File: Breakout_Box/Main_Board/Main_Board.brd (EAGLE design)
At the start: 60 x 100 mm, 18 parts, among them CN1 19PIN_LEMO

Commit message: Licenses
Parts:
- added U$1: TH-PAD-1.6/0.8, CYCFI_Con:TH-PAD-1.6/0.8
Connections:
- net AGND: now also U$1.1
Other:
- board text added: "H14"
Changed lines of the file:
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@@
 <board>
 <plain>
-<wire x1="0" y1="0" x2="60" y2="0" width="0" layer="20"/>
-<wire x1="60" y1="0" x2="60" y2="100" width="0" layer="20"/>
-<wire x1="60" y1="100" x2="0" y2="100" width="0" layer="20"/>
-<wire x1="0" y1="100" x2="0" y2="0" width="0" layer="20"/>
+<wire x1="0" y1="0" x2="60" y2="0" width="0.1" layer="20"/>
+<wire x1="60" y1="0" x2="60" y2="100" width="0.1" layer="20"/>
+<wire x1="60" y1="100" x2="0" y2="100" width="0.1" layer="20"/>
+<wire x1="0" y1="100" x2="0" y2="0" width="0.1" layer="20"/>
 <text x="53.5" y="16.8" size="0.8128" layer="25" ratio="10">+</text>
 <text x="53.5" y="14.4" size="0.8128" layer="25" ratio="10">-</text>
@@
 <text x="9.70000625" y="5.6999875" size="0.8128" layer="125" ratio="10">LED1</text>
 <text x="7.114996875" y="11.562003125" size="0.8128" layer="125" ratio="10">R2</text>
+<text x="52.95" y="12.795" size="0.8128" layer="25" ratio="10" distance="46">H14</text>
 </plain>
 <attributes>
@@
 <attribute name="NAME" x="47.0225" y="14.975" size="0.8128" layer="21" ratio="10"/>
 </element>
+<element name="U$1" library="CYCFI_Con" package="TH-PAD-1.6/0.8" value="TH-PAD-1.6/0.8" x="13.5" y="3.5" smashed="yes">
+<attribute name="VALUE" x="13.5" y="4.1" size="0.0254" layer="27"/>
+</element>
 </elements>
 <signals>
@@
 <wire x1="10.75" y1="14.5" x2="12.25" y2="13" width="0.4064" layer="1"/>
 <wire x1="12.25" y1="13" x2="20" y2="13" width="0.4064" layer="1"/>
+<contactref element="U$1" pad="1"/>
 </signal>
 <signal name="DGND">

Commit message: *Edit Logo *Check BOM *Added 19P Connector Files
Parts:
- GND: value TH-PAD-1.6/0.8 -> (none)
- renumbered U$1 to GND
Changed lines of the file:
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@@
 <attribute name="NAME" x="47.0225" y="14.975" size="0.8128" layer="21" ratio="10"/>
 </element>
-<element name="U$1" library="CYCFI_Con" package="TH-PAD-1.6/0.8" value="TH-PAD-1.6/0.8" x="13.5" y="3.5" smashed="yes">
+<element name="GND" library="CYCFI_Con" package="TH-PAD-1.6/0.8" value="" x="13.5" y="3.5" smashed="yes">
 <attribute name="VALUE" x="13.5" y="4.1" size="0.0254" layer="27"/>
 </element>
@@
 <wire x1="10.75" y1="14.5" x2="12.25" y2="13" width="0.4064" layer="1"/>
 <wire x1="12.25" y1="13" x2="20" y2="13" width="0.4064" layer="1"/>
-<contactref element="U$1" pad="1"/>
+<contactref element="GND" pad="1"/>
 </signal>
 <signal name="DGND">

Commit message: reset devel
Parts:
- added C1, C3: 22uF, resistor:C0805
- added C4: 1uF, resistor:C0603
- added C5: 10uF, resistor:C0603
- added C7: 1nF, resistor:C0402K
- added H3, H4, H5: (no value), con-lstb:MA03-1_
- added L2: 82uH, resistor:L1280
- added Q1: DMP3099L, CYCFI_semicon:SOT23
- added Q2: DSS6060, CYCFI_semicon:SOT-223-4
- added R1: 1k, resistor:R0402
- C2: value 0.1uF -> 470uF; device resistor:C0603 -> resistor:140CLH-1010
- D1: value FM4007W -> FM4004W
- L1: value 100uH -> 1mH; device resistor:L1280 -> inductors:SDR
- moved D1 47.3 mm to (32.5, 60.8), turned to 90 degrees
- moved H1 45.6 mm to (50.0, 71.0)
- moved H2 45.6 mm to (9.00, 71.0)
- moved C2 42.4 mm to (28.3, 49.6), turned to 0 degrees
- moved L1 30.2 mm to (43.0, 36.5), turned to 90 degrees
- moved H13 28.7 mm to (12.8, 29.8), turned to 0 degrees
- moved C6 27.9 mm to (29.2, 24.5)
- moved H12 25.3 mm to (12.8, 27.0), turned to 0 degrees
- moved H11 22.2 mm to (12.8, 24.2), turned to 0 degrees
- moved H8 20.0 mm to (57.0, 103.2)
- moved H9 20.0 mm to (57.0, 81.8)
- moved H10 19.3 mm to (12.8, 21.5), turned to 0 degrees
- moved H6 18.0 mm to (17.5, 112.5)
- moved H7 18.0 mm to (39.0, 112.5)
- moved H14 17.0 mm to (56.0, 33.0)
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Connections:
- removed net +12V_REG: C2.1, C6.+, CN1.P$16, H1.10, H1.11, H1.8, H1.9, H9.1, H9.2, H9.3, H9.4, L1.P$2, R2.1
- removed net AGND: C2.2, C6.-, CN1.P$19, GND.1, H1.16, H1.17, H1.18, H1.19, H14.1, H7.5, H7.6, H7.7, H7.8, LED1.K
- removed net DGND: H1.12, H1.13, H1.14, H1.15, H9.5, H9.6, H9.7, H9.8
- removed net N$22: H2.19
- removed net N$23: H2.20
- removed net N$24: H1.20
- removed net N$26 (its old number): CN1.P$18
- removed net N$31: D1.CATHODE, L1.P$1
- removed net N$60: CN1.P$13, H1.5, H8.5
- removed net N$61: CN1.P$14, H1.6, H8.6
- removed net N$62: CN1.P$15, H1.7, H8.7
- removed net N$9 (its old number): CN1.P$17
- new net +AVCC: C4.1, C5.1, C7.1, CN1.P$16, CN1.P$17, D1.ANODE, H1.14, H1.15, H9.1, H9.2, Q2.P$3, R2.1
- new net +DVCC: C3.1, H1.8, H1.9, H9.5, H9.6, L1.P$2
- new net GND: C1.2, C2.-, C3.2, C4.2, C5.2, C6.-, C7.2, CN1.P$18, CN1.P$19, GND.1, H1.10, H1.11, H1.12, H1.13, H1.16, H1.17, H1.18, H1.19, H14.1, H2.16, H2.17, H2.18, H2.19, H2.20, H7.5, H7.6, H7.7, H7.8, H9.3, H9.4, H9.7, H9.8, LED1.K, Q1.1
- new net N$33: H1.5, H3.3, H8.5
- new net N$34: H1.6, H4.3, H8.6
- new net N$35: H1.7, H5.3, H8.7
- new net N$36: CN1.P$13, H3.2
- new net N$37: CN1.P$14, H4.2
- new net N$38: CN1.P$15, H5.2
- net N$1: now also H3.1
- net N$17: now also H5.1
- net N$19: now also C1.1, L1.P$1, L2.P$1, Q1.2; no longer H2.16
- net N$2: now also Q1.3; no longer D1.ANODE
- net N$20: now also C2.+, Q2.P$1, R1.1; no longer H2.17
- net N$21: now also C6.+, D1.CATHODE, L2.P$2, Q2.P$2, Q2.P$4, R1.2; no longer H2.18
- net N$3: now also H4.1
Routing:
- net N$17: track 0.00 -> 208.6 mm
- net N$3: track 0.00 -> 207.4 mm
- net N$1: track 0.00 -> 201.4 mm
- net +12V_REG: track 195.9 -> 0.00 mm, vias 1 -> 0
- net N$35: track 0.00 -> 179.9 mm, vias 0 -> 1
- net N$34: track 0.00 -> 175.0 mm, vias 0 -> 1
- net +AVCC: track 0.00 -> 169.7 mm, vias 0 -> 1
- net N$33: track 0.00 -> 169.7 mm, vias 0 -> 1
- net N$60: track 117.6 -> 0.00 mm, vias 2 -> 0
- net N$61: track 116.7 -> 0.00 mm, vias 2 -> 0
- net N$62: track 114.9 -> 0.00 mm
- net N$28: track 100.4 -> 197.6 mm, vias 1 -> 0
- net N$29: track 110.9 -> 191.9 mm, vias 1 -> 0
- net N$37: track 0.00 -> 72.6 mm, vias 0 -> 1
- net N$18: track 115.3 -> 187.2 mm, vias 1 -> 0
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- added copper zone on layer 16, net GND
- added copper zone on layer 16, net N$22
- added copper zone on layer 16, net N$23
- removed copper zone on layer 1, net AGND
- removed copper zone on layer 16, net AGND
- removed copper zone on layer 1, net DGND
- removed copper zone on layer 16, net DGND
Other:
- board size 60 x 100 mm -> 60 x 120 mm
- board text added: "+V_IN"
- board text added: "AVCC"
- board text added: "CH13"
- board text added: "CH13_A"
- board text added: "CH14"
- board text added: "CH14_A"
- board text added: "CH15"
- board text added: "CH15_A"
- board text added: "DVCC"
- board text added: "L1"
- board text added: "L2"
- board text added: "Nexus Main Board"
- board text added: "Q2"
- board text added: "v0.96"
- board text removed: "+12V_REG"
- board text removed: "12V"
- board text removed: "C2"
- board text removed: "C6"
- board text removed: "D1"
- board text removed: "H1"
- board text removed: "H2"
- board text removed: "H6"
- board text removed: "H7"
- board text removed: "H8"
- board text removed: "H9"
- board text removed: "LED1"
- board text removed: "R2"
- board text removed: "v0.9"

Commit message: merge version_1.1 to devel
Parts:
- removed C1, C3: 22uF, resistor:C0805
- removed C4: 1uF, resistor:C0603
- removed C5: 10uF, resistor:C0603
- removed C7: 1nF, resistor:C0402K
- removed H3, H4, H5: (no value), con-lstb:MA03-1_
- removed L2: 82uH, resistor:L1280
- removed Q1: DMP3099L, CYCFI_semicon:SOT23
- removed Q2: DSS6060, CYCFI_semicon:SOT-223-4
- removed R1: 1k, resistor:R0402
- C2: value 470uF -> 0.1uF; device resistor:140CLH-1010 -> resistor:C0603
- D1: value FM4004W -> FM4007W
- L1: value 1mH -> 100uH; device inductors:SDR -> resistor:L1280
- moved D1 47.3 mm to (50.0, 16.8), turned to 270 degrees
- moved H1 45.6 mm to (9.00, 51.0)
- moved H2 45.6 mm to (50.0, 51.0)
- moved C2 42.4 mm to (43.5, 10.0), turned to 90 degrees
- moved L1 30.2 mm to (35.5, 7.25), turned to 0 degrees
- moved H13 28.7 mm to (39.6, 19.6), turned to 90 degrees
- moved C6 27.9 mm to (51.0, 7.00)
- moved H12 25.3 mm to (37.0, 19.6), turned to 90 degrees
- moved H11 22.2 mm to (34.5, 19.6), turned to 90 degrees
- moved H8 20.0 mm to (57.0, 83.2)
- moved H9 20.0 mm to (57.0, 61.8)
- moved H10 19.3 mm to (31.9, 19.6), turned to 90 degrees
- moved H6 18.0 mm to (17.5, 94.5)
- moved H7 18.0 mm to (39.0, 94.5)
- moved H14 17.0 mm to (56.0, 16.0)
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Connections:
- removed net +AVCC: C4.1, C5.1, C7.1, CN1.P$16, CN1.P$17, D1.ANODE, H1.14, H1.15, H9.1, H9.2, Q2.P$3, R2.1
- removed net +DVCC: C3.1, H1.8, H1.9, H9.5, H9.6, L1.P$2
- removed net GND: C1.2, C2.-, C3.2, C4.2, C5.2, C6.-, C7.2, CN1.P$18, CN1.P$19, GND.1, H1.10, H1.11, H1.12, H1.13, H1.16, H1.17, H1.18, H1.19, H14.1, H2.16, H2.17, H2.18, H2.19, H2.20, H7.5, H7.6, H7.7, H7.8, H9.3, H9.4, H9.7, H9.8, LED1.K, Q1.1
- removed net N$33: H1.5, H3.3, H8.5
- removed net N$34: H1.6, H4.3, H8.6
- removed net N$35: H1.7, H5.3, H8.7
- removed net N$36: CN1.P$13, H3.2
- removed net N$37: CN1.P$14, H4.2
- removed net N$38: CN1.P$15, H5.2
- new net +12V_REG: C2.1, C6.+, CN1.P$16, H1.10, H1.11, H1.8, H1.9, H9.1, H9.2, H9.3, H9.4, L1.P$2, R2.1
- new net AGND: C2.2, C6.-, CN1.P$19, GND.1, H1.16, H1.17, H1.18, H1.19, H14.1, H7.5, H7.6, H7.7, H7.8, LED1.K
- new net DGND: H1.12, H1.13, H1.14, H1.15, H9.5, H9.6, H9.7, H9.8
- new net N$22: H2.19
- new net N$23: H2.20
- new net N$24: H1.20
- new net N$26: CN1.P$18
- new net N$31: D1.CATHODE, L1.P$1
- new net N$60: CN1.P$13, H1.5, H8.5
- new net N$61: CN1.P$14, H1.6, H8.6
- new net N$62: CN1.P$15, H1.7, H8.7
- new net N$9: CN1.P$17
- net N$1: no longer H3.1
- net N$17: no longer H5.1
- net N$19: now also H2.16; no longer C1.1, L1.P$1, L2.P$1, Q1.2
- net N$2: now also D1.ANODE; no longer Q1.3
- net N$20: now also H2.17; no longer C2.+, Q2.P$1, R1.1
- net N$21: now also H2.18; no longer C6.+, D1.CATHODE, L2.P$2, Q2.P$2, Q2.P$4, R1.2
- net N$3: no longer H4.1
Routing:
- net N$17: track 208.6 -> 0.00 mm
- net N$3: track 207.4 -> 0.00 mm
- net N$1: track 201.4 -> 0.00 mm
- net +12V_REG: track 0.00 -> 195.9 mm, vias 0 -> 1
- net N$35: track 179.9 -> 0.00 mm, vias 1 -> 0
- net N$34: track 175.0 -> 0.00 mm, vias 1 -> 0
- net +AVCC: track 169.7 -> 0.00 mm, vias 1 -> 0
- net N$33: track 169.7 -> 0.00 mm, vias 1 -> 0
- net N$60: track 0.00 -> 117.6 mm, vias 0 -> 2
- net N$61: track 0.00 -> 116.7 mm, vias 0 -> 2
- net N$62: track 0.00 -> 114.9 mm
- net N$28: track 197.6 -> 100.4 mm, vias 0 -> 1
- net N$29: track 191.9 -> 110.9 mm, vias 0 -> 1
- net N$37: track 72.6 -> 0.00 mm, vias 1 -> 0
- net N$18: track 187.2 -> 115.3 mm, vias 0 -> 1
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- added copper zone on layer 1, net AGND
- added copper zone on layer 16, net AGND
- added copper zone on layer 1, net DGND
- added copper zone on layer 16, net DGND
- removed copper zone on layer 16, net GND
- removed copper zone on layer 16, net N$22
- removed copper zone on layer 16, net N$23
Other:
- board size 60 x 120 mm -> 60 x 100 mm
- board text added: "+12V_REG"
- board text added: "12V"
- board text added: "C2"
- board text added: "C6"
- board text added: "D1"
- board text added: "H1"
- board text added: "H2"
- board text added: "H6"
- board text added: "H7"
- board text added: "H8"
- board text added: "H9"
- board text added: "LED1"
- board text added: "R2"
- board text added: "v0.9"
- board text removed: "+V_IN"
- board text removed: "AVCC"
- board text removed: "CH13"
- board text removed: "CH13_A"
- board text removed: "CH14"
- board text removed: "CH14_A"
- board text removed: "CH15"
- board text removed: "CH15_A"
- board text removed: "DVCC"
- board text removed: "L1"
- board text removed: "L2"
- board text removed: "Nexus Main Board"
- board text removed: "Q2"
- board text removed: "v0.96"

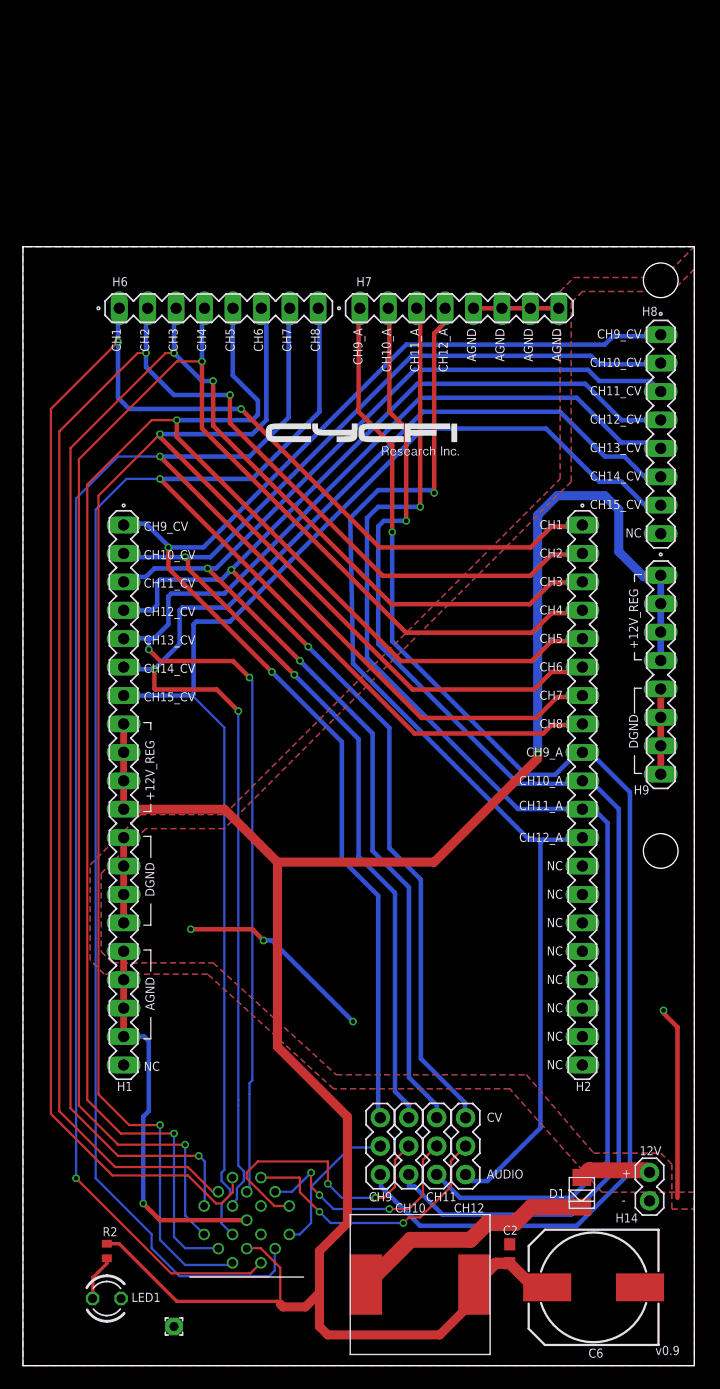
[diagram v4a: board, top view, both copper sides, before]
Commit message: Create version_2.0 with updated main and midi modules
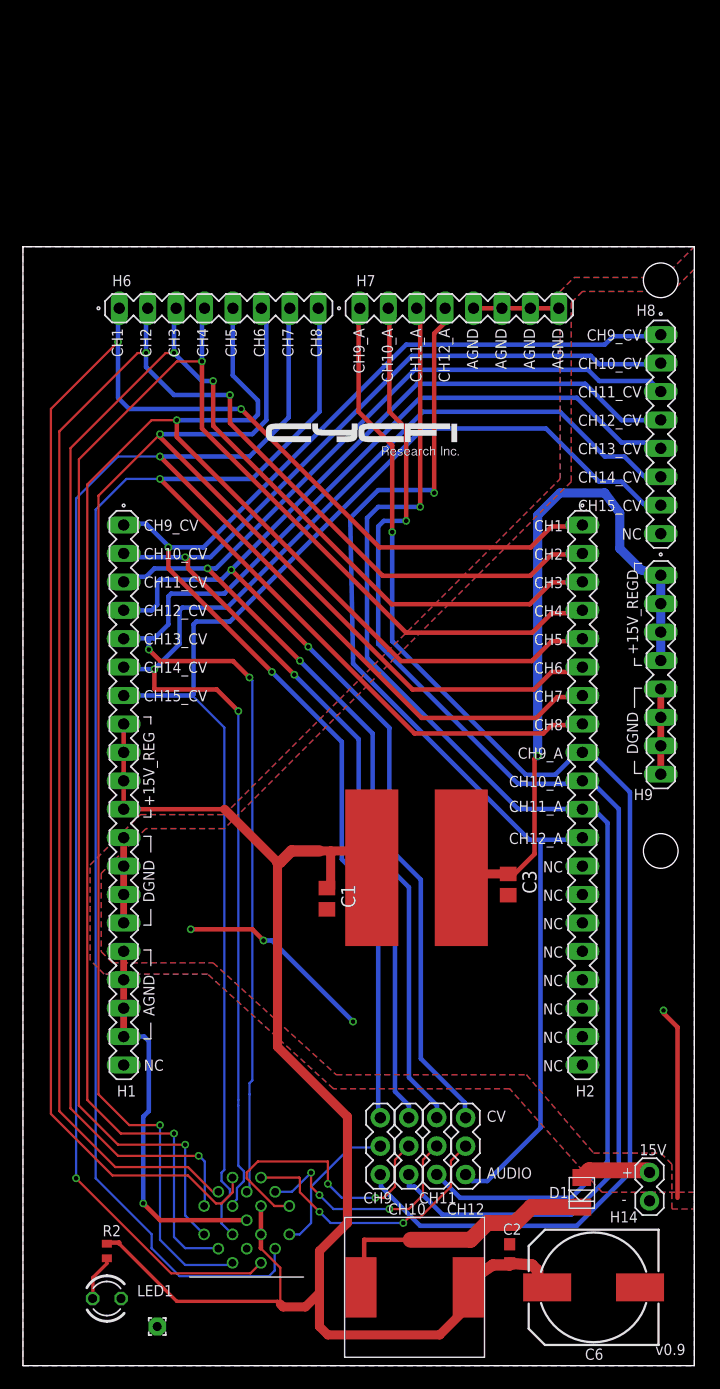
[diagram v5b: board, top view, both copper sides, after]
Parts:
- added C1, C3: 22uF, resistor:C0805
- added L2: 100uH, resistor:L1280
- L1: value 100uH -> 100mH; device resistor:L1280 -> inductors:SDR
- moved L1 37.8 mm to (35.2, 45.0)
- moved GND 1.50 mm to (12.0, 3.50)
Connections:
- removed net +12V_REG: C2.1, C6.+, CN1.P$16, H1.10, H1.11, H1.8, H1.9, H9.1, H9.2, H9.3, H9.4, L1.P$2, R2.1
- removed net N$26: CN1.P$18
- removed net N$9: CN1.P$17
- new net +15V_REG: C1.1, C2.1, C6.+, CN1.P$17, CN1.P$18, H1.10, H1.11, H1.8, H1.9, L1.P$1, L2.P$2, R2.1
- new net +15V_REGD: C3.1, H9.1, H9.2, H9.3, H9.4, L1.P$2
- new net NC: CN1.P$16
- net DGND: now also C1.2, C3.2
- net N$31: now also L2.P$1; no longer L1.P$1
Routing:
- net +12V_REG: track 195.9 -> 0.00 mm, vias 1 -> 0
- net +15V_REG: track 0.00 -> 142.3 mm
- net +15V_REGD: track 0.00 -> 62.6 mm, vias 0 -> 1
- net N$31: track 22.2 -> 25.3 mm
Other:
- board text added: "+15V_REG"
- board text added: "+15V_REGD"
- board text added: "15V"
- board text removed: "+12V_REG"
- board text removed: "12V"
- board text removed: "C2"
- board text removed: "C6"
- board text removed: "D1"
- board text removed: "H1"
- board text removed: "H2"
- board text removed: "H6"
- board text removed: "H7"
- board text removed: "H8"
- board text removed: "H9"
- board text removed: "LED1"
- board text removed: "R2"
